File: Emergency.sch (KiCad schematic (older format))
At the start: 16 parts, among them J21 EMERGENCY, J22 EPSON POWER IN, J23 EPSON BOARD POWER, K1 S13-24V-2C, Q7 BC817, U8 74HC2G32

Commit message: Shematic almost finished, BOM in KiCad 3/4 finished
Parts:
- D29: renamed from D30; footprint (none) -> Diode_SMD:D_SOD-323; Cena (none) -> 0.14905; Link (none) -> https://www.tme.eu/pl/details/1n4448ws-7-f/diody-uniwersaln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; Model (none) -> 1N4448WS-7-F; Opis (none) -> Dioda: prostownicza; SMD; 75V; 0,25A; 4ns;; Producent (none) -> DIODES INCORPORATED; Typ (none) -> SMD
- D30: renamed from D29; Cena (none) -> 0.14905; Link (none) -> https://www.tme.eu/pl/details/1n4448ws-7-f/diody-uniwersaln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; Model (none) -> 1N4448WS-7-F; Opis (none) -> Dioda: prostownicza; SMD; 75V; 0,25A; 4ns;; Producent (none) -> DIODES INCORPORATED; Typ (none) -> SMD
- D31: Cena (none) -> 0.14905; Link (none) -> https://www.tme.eu/pl/details/1n4448ws-7-f/diody-uniwersaln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; Model (none) -> 1N4448WS-7-F; Opis (none) -> Dioda: prostownicza; SMD; 75V; 0,25A; 4ns;; Producent (none) -> DIODES INCORPORATED; Typ (none) -> SMD
- F6: Cena (none) -> 0.3763; Link (none) -> https://www.tme.eu/pl/details/sn010-60/bezpieczniki-polimer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; Model (none) -> SN010-60; Opis (none) -> Bezpiecznik: polimerowy PTC; 100mA; Obud: 1206; Producent (none) -> ECE; Typ (none) -> SMD
- J21: Cena (none) -> 0.47429; Link (none) -> https://www.tme.eu/pl/details/b2b-ph-k-s/zlacza-sygnalowe-r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; Model (none) -> B2B-PH-K-S; Opis (none) -> Gniazdo; przewód-płytka; męskie; PH; 2mm; PIN: 2; THT; 100V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; Producent (none) -> JST; Typ (none) -> THT
- J22, J23: footprint Connector_JST:JST_PH_B2B-PH-K_1x03_P2.00mm_Vertical -> Connector_JST:JST_PH_B3B-PH-K_1x03_P2.00mm_Vertical; Cena (none) -> 0.59599; Link (none) -> https://www.tme.eu/pl/details/b3b-ph-k-s/zlacza-sygnalowe-r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; Model (none) -> B3B-PH-K-S; Opis (none) -> Gniazdo; przewód-płytka; męskie; PH; 2mm; PIN: 3; THT; 100V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; Producent (none) -> JST; Typ (none) -> THT
- R55: renamed from R56; footprint (none) -> Resistor_SMD:R_0805_2012Metric
- R56: renamed from R57; footprint (none) -> Resistor_SMD:R_0603_1608Metric
- R57: renamed from R55; footprint (none) -> Resistor_SMD:R_0603_1608Metric
- R58, R59: footprint (none) -> Resistor_SMD:R_0603_1608Metric
- U8: Cena (none) -> 1.1252; Link (none) -> https://www.tme.eu/pl/details/74hc2g32dc.125/bramki-inwerte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; Model (none) -> 74HC2G32DC.125; Opis (none) -> IC: cyfrowy; OR; Kanały: 2; IN: 4; CMOS; SMD; VSSOP8; Seria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; Producent (none) -> NEXPERIA; Typ (none) -> SMD
- renumbered C60 to C62

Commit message: BOM in KiCad almost finished, genereated NETLIST, create PCB
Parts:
- C62: Cena (none) -> 0.05563; Link (none) -> https://www.tme.eu/pl/details/cl10b102kb8nnnc/kondensatory-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; Model (none) -> CL10B102KB8NNNC; Opis (none) -> Kondensator: ceramiczny; MLCC; 1nF; 50V; X7R; ±10%; SMD; 06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; Producent (none) -> SAMSUNG; Typ (none) -> SMD
- K1: Cena (none) -> 4.46; Link (none) -> https://www.tme.eu/pl/details/s13-24v-2c/przekazniki-elektr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; Model (none) -> S13-24V-2C; Opis (none) -> Przekaźnik: elektromagnetyczny; DPDT; Ucewki : 24VDC; 0,5A/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; Producent (none) -> SHORI ELECTRIC; Typ (none) -> THT
- Q7: Cena (none) -> 0.1189; Link (none) -> https://www.tme.eu/pl/details/bc817.215/tranzystory-npn-smd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; Model (none) -> BC817.215; Opis (none) -> Tranzystor: NPN; bipolarny; 45V; 0,5A; 250mW; SOT23; Producent (none) -> NEXPERIA; Typ (none) -> SMD
- R55, R56, R58, R59: Cena (none) -> 0.04651; Typ (none) -> SMD
- R57: Cena (none) -> 0.04651; Link (none) -> https://www.tme.eu/pl/details/smd0603-1k-1%25/rezystory-smd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; Model (none) -> 0603SAF1001T5E; Opis (none) -> Rezystor: thick film; SMD; 0603; 1kΩ; 0,1W; ±1%; -55÷155°C; Producent (none) -> ROYAL OHM; Typ (none) -> SMD
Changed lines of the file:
@@
 F 2 "footprints:Relay_DPDT_Omron_G5V-2" H 4050 3600 50  0001 L CNN
 F 3 "https://www.tme.eu/Document/64152b8fe9c340a87eeb0f5deb8b7f91/s13-relay.pdf" H 4050 3600 50  0001 C CNN
+F 4 "4.46" H 4050 3600 50  0001 C CNN "Cena"
+F 5 "https://www.tme.eu/pl/details/s13-24v-2c/przekazniki-elektromagn-miniaturowe/shori-electric/" H 4050 3600 50  0001 C CNN "Link"
+F 6 "S13-24V-2C" H 4050 3600 50  0001 C CNN "Model"
+F 7 "Przekaźnik: elektromagnetyczny; DPDT; Ucewki : 24VDC; 0,5A/125VAC" H 4050 3600 50  0001 C CNN "Opis"
+F 8 "SHORI ELECTRIC" H 4050 3600 50  0001 C CNN "Producent"
+F 9 "THT" H 4050 3600 50  0001 C CNN "Typ"
 	1    4050 3600
 	0    1    1    0
@@
 F 2 "Resistor_SMD:R_0603_1608Metric" V 5930 2350 50  0001 C CNN
 F 3 "~" H 6000 2350 50  0001 C CNN
+F 4 "0.04651" H 6000 2350 50  0001 C CNN "Cena"
+F 5 "SMD" H 6000 2350 50  0001 C CNN "Typ"
 	1    6000 2350
 	0    1    1    0
@@
 F 2 "Package_TO_SOT_SMD:SOT-23" H 6750 2275 50  0001 L CIN
 F 3 "http://www.fairchildsemi.com/ds/BC/BC817.pdf" H 6550 2350 50  0001 L CNN
+F 4 "0.1189" H 6550 2350 50  0001 C CNN "Cena"
+F 5 "https://www.tme.eu/pl/details/bc817.215/tranzystory-npn-smd/nexperia/" H 6550 2350 50  0001 C CNN "Link"
+F 6 "BC817.215" H 6550 2350 50  0001 C CNN "Model"
+F 7 "Tranzystor: NPN; bipolarny; 45V; 0,5A; 250mW; SOT23" H 6550 2350 50  0001 C CNN "Opis"
+F 8 "NEXPERIA" H 6550 2350 50  0001 C CNN "Producent"
+F 9 "SMD" H 6550 2350 50  0001 C CNN "Typ"
 	1    6550 2350
 	1    0    0    -1
@@
 F 2 "Resistor_SMD:R_0603_1608Metric" V 6580 1900 50  0001 C CNN
 F 3 "~" H 6650 1900 50  0001 C CNN
+F 4 "0.04651" H 6650 1900 50  0001 C CNN "Cena"
+F 5 "https://www.tme.eu/pl/details/smd0603-1k-1%25/rezystory-smd-0603/royal-ohm/0603saf1001t5e/" H 6650 1900 50  0001 C CNN "Link"
+F 6 "0603SAF1001T5E" H 6650 1900 50  0001 C CNN "Model"
+F 7 "Rezystor: thick film; SMD; 0603; 1kΩ; 0,1W; ±1%; -55÷155°C" H 6650 1900 50  0001 C CNN "Opis"
+F 8 "ROYAL OHM" H 6650 1900 50  0001 C CNN "Producent"
+F 9 "SMD" H 6650 1900 50  0001 C CNN "Typ"
 	1    6650 1900
 	1    0    0    -1
@@
 F 2 "Resistor_SMD:R_0805_2012Metric" V 5080 2350 50  0001 C CNN
 F 3 "~" H 5150 2350 50  0001 C CNN
+F 4 "0.04651" H 5150 2350 50  0001 C CNN "Cena"
+F 5 "SMD" H 5150 2350 50  0001 C CNN "Typ"
 	1    5150 2350
 	0    1    1    0
@@
 F 2 "Resistor_SMD:R_0603_1608Metric" V 7580 3950 50  0001 C CNN
 F 3 "~" H 7650 3950 50  0001 C CNN
+F 4 "0.04651" H 7650 3950 50  0001 C CNN "Cena"
+F 5 "SMD" H 7650 3950 50  0001 C CNN "Typ"
 	1    7650 3950
 	1    0    0    -1
@@
 F 2 "Resistor_SMD:R_0603_1608Metric" V 7580 3200 50  0001 C CNN
 F 3 "~" H 7650 3200 50  0001 C CNN
+F 4 "0.04651" H 7650 3200 50  0001 C CNN "Cena"
+F 5 "SMD" H 7650 3200 50  0001 C CNN "Typ"
 	1    7650 3200
 	1    0    0    -1
@@
 F 2 "Capacitor_SMD:C_0603_1608Metric" H 7200 2350 50  0001 C CNN
 F 3 "~" H 7200 2350 50  0001 C CNN
+F 4 "0.05563" H 7200 2350 50  0001 C CNN "Cena"
+F 5 "https://www.tme.eu/pl/details/cl10b102kb8nnnc/kondensatory-mlcc-smd-0603/samsung/" H 7200 2350 50  0001 C CNN "Link"
+F 6 "CL10B102KB8NNNC" H 7200 2350 50  0001 C CNN "Model"
+F 7 "Kondensator: ceramiczny; MLCC; 1nF; 50V; X7R; ±10%; SMD; 0603" H 7200 2350 50  0001 C CNN "Opis"
+F 8 "SAMSUNG" H 7200 2350 50  0001 C CNN "Producent"
+F 9 "SMD" H 7200 2350 50  0001 C CNN "Typ"
 	1    7200 2350
 	1    0    0    -1

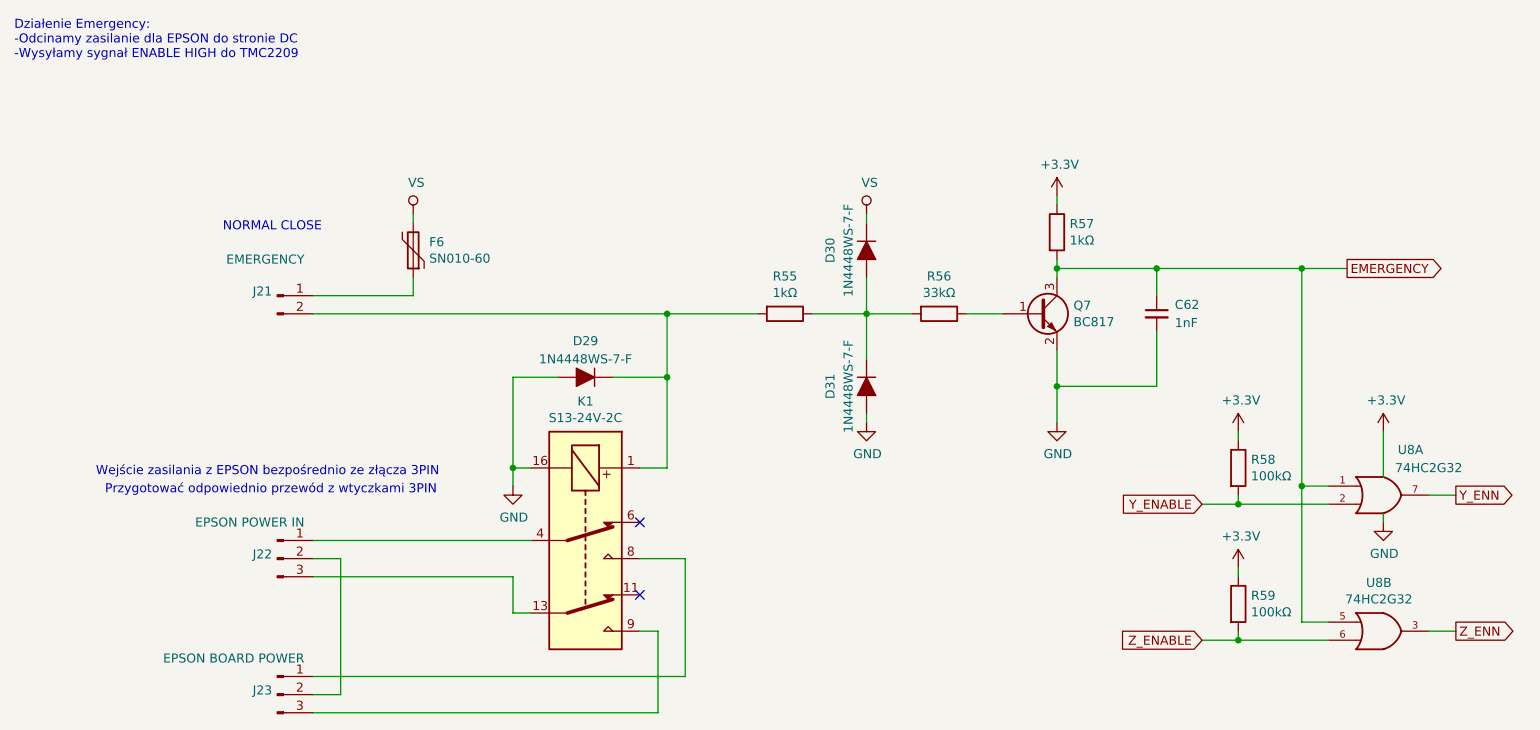
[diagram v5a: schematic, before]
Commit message: Improve Emergency, Added TVS diodes
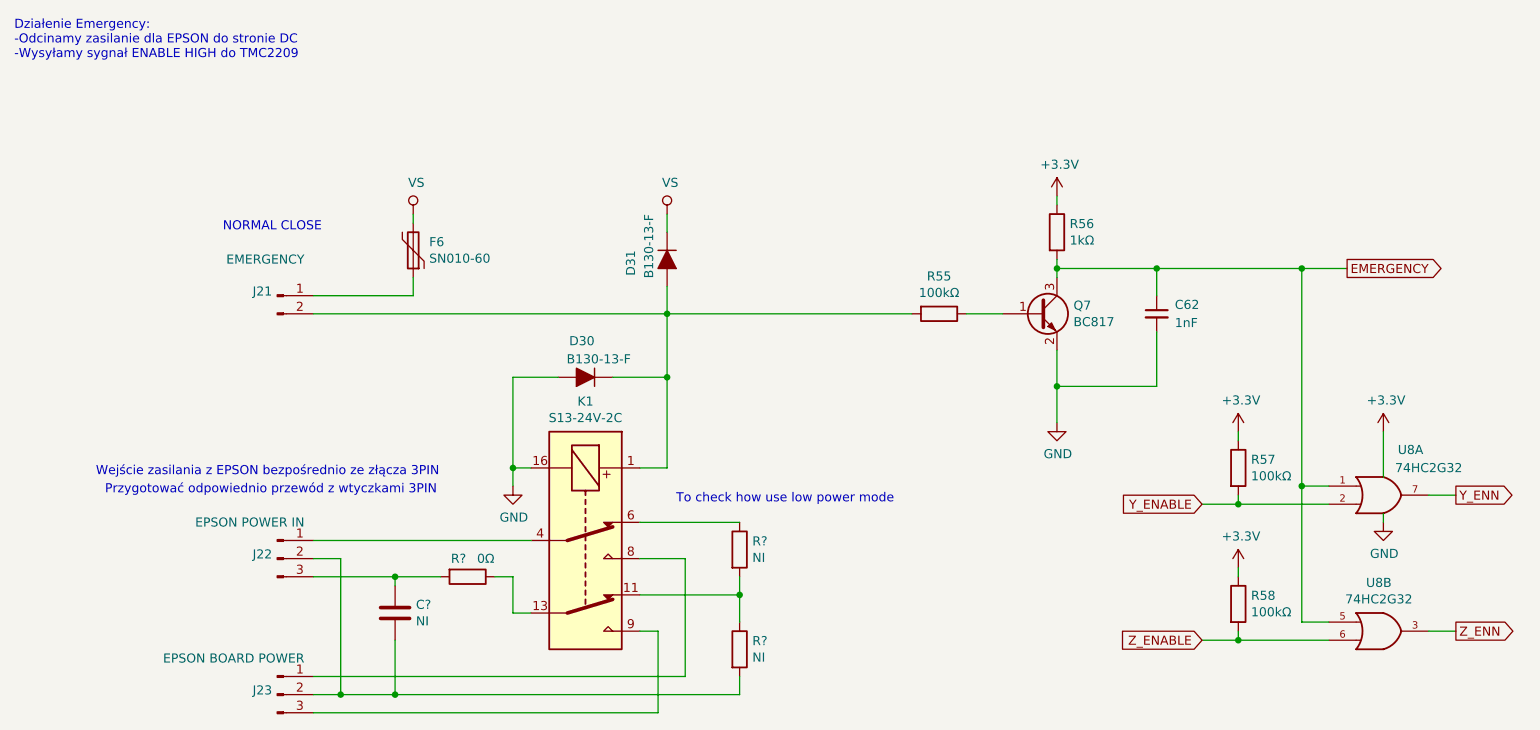
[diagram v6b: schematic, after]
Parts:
- removed D29: 1N4448WS-7-F, Diode_SMD:D_SOD-323, symbol Device:D_ALT
- removed R55: 1kΩ, Resistor_SMD:R_0805_2012Metric, symbol Device:R
- added C?: NI, Capacitor_SMD:C_0805_2012Metric, symbol Device:C
- added R? (x2): NI, Resistor_SMD:R_0805_2012Metric, symbol Device:R
- added R?: 0Ω, Resistor_SMD:R_0805_2012Metric, symbol Device:R
- D30, D31: value 1N4448WS-7-F -> B130-13-F; footprint Diode_SMD:D_SOD-323 -> Diode_SMD:D_SMA; Cena 0.14905 -> 0.29301; Link https://www.tme.eu/pl/details/1n4448ws-7-f/diody-uniwersaln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 -> https://www.tme.eu/pl/details/b130-13-f/diody-schottky-smd/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; Model 1N4448WS-7-F -> B130-13-F; Opis Dioda: prostownicza; SMD; 75V; 0,25A; 4ns; -> Dioda: prostownicza Schottky; SMD; 40V; 1A; SMA
- R55: renamed from R56; value 33kΩ -> 100kΩ
- renumbered R57 to R56, R58 to R57, R59 to R58
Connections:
- net GND: now also D30.2 (A); no longer D31.2 (A)
- net VS: now also D31.1 (K); no longer D30.1 (K)
- net at J21.2 (Pin_2), K1.1: now also D30.1 (K), D31.2 (A), R55.2
- net at K1.11: now also R?.1, R?.2
- net at K1.13: now also R?.1; no longer J22.3 (Pin_3)
- net at K1.6: now also R?.1
- net at J22.2 (Pin_2), J23.2 (Pin_2): now also C?.2, R?.2
- new net: C?.1, J22.3 (Pin_3), R?.2
- no-connect marks 2 -> 0
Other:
- note added: "To check how use low power mode"
